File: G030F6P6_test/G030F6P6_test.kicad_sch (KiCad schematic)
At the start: 36 parts, among them J1 Conn_01x10_Female, J3 Conn_01x10_Female, J4 USB_C_Receptacle_USB2.0, J5 Conn_01x05_Female, SW1 SW_Push_SPDT, U1 CH343P, U2 STM32G030FxP, U3 XC6206P332MR

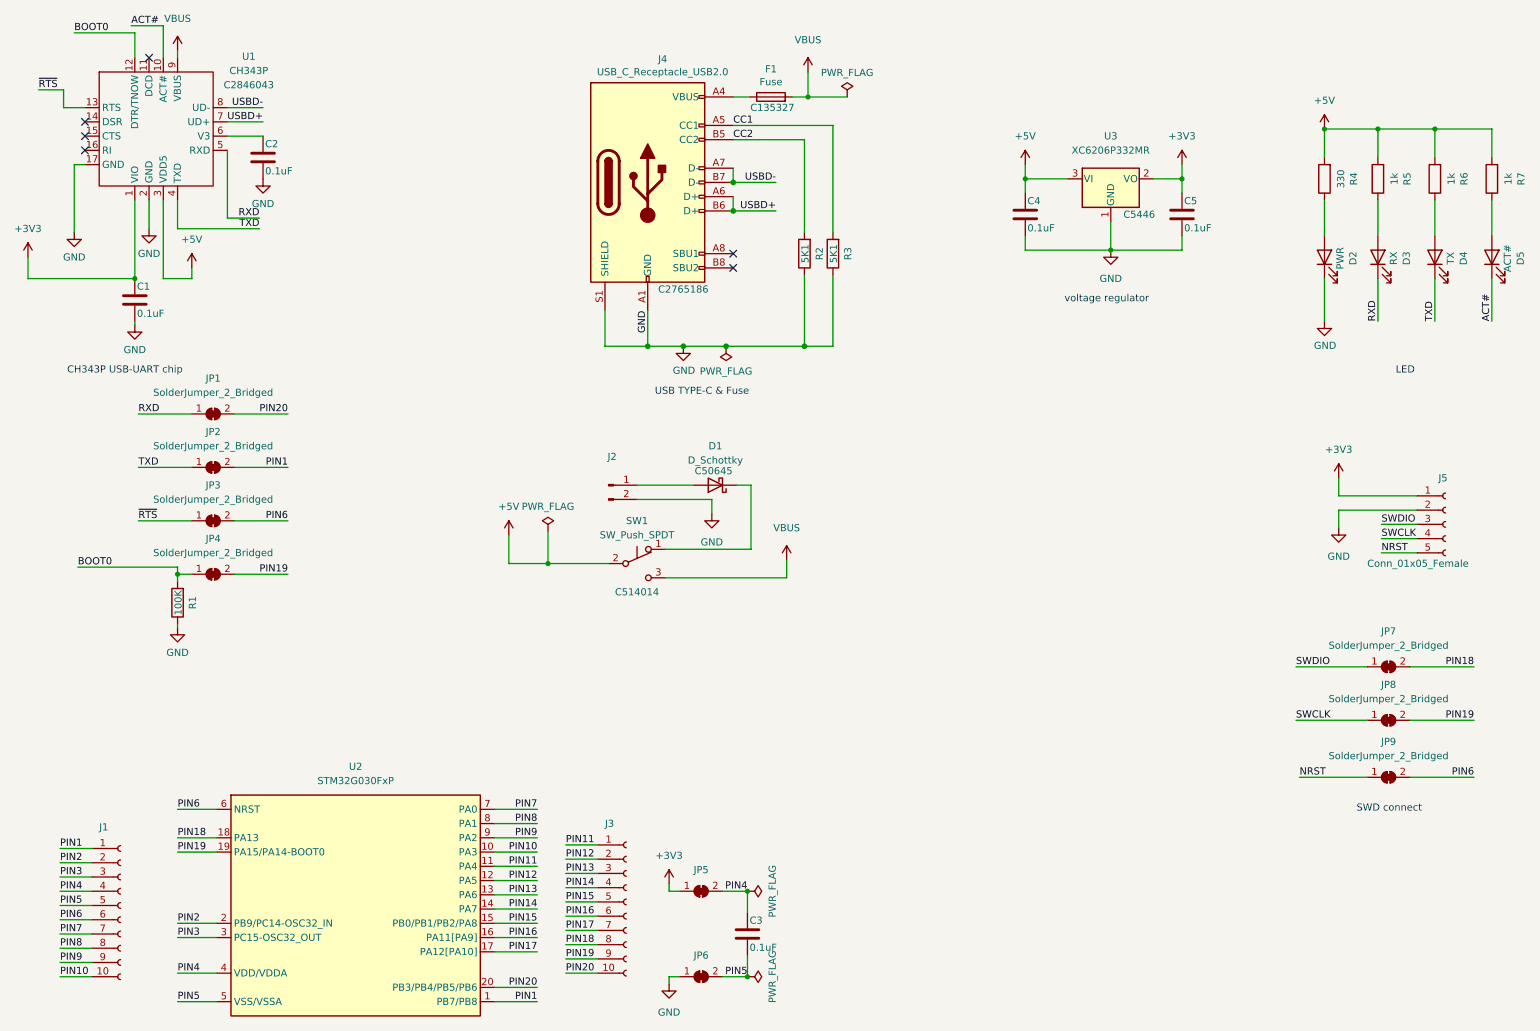
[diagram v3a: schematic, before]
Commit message: Update G030F6P6_test.kicad_sch
移除LED
更換 CH343P 封裝
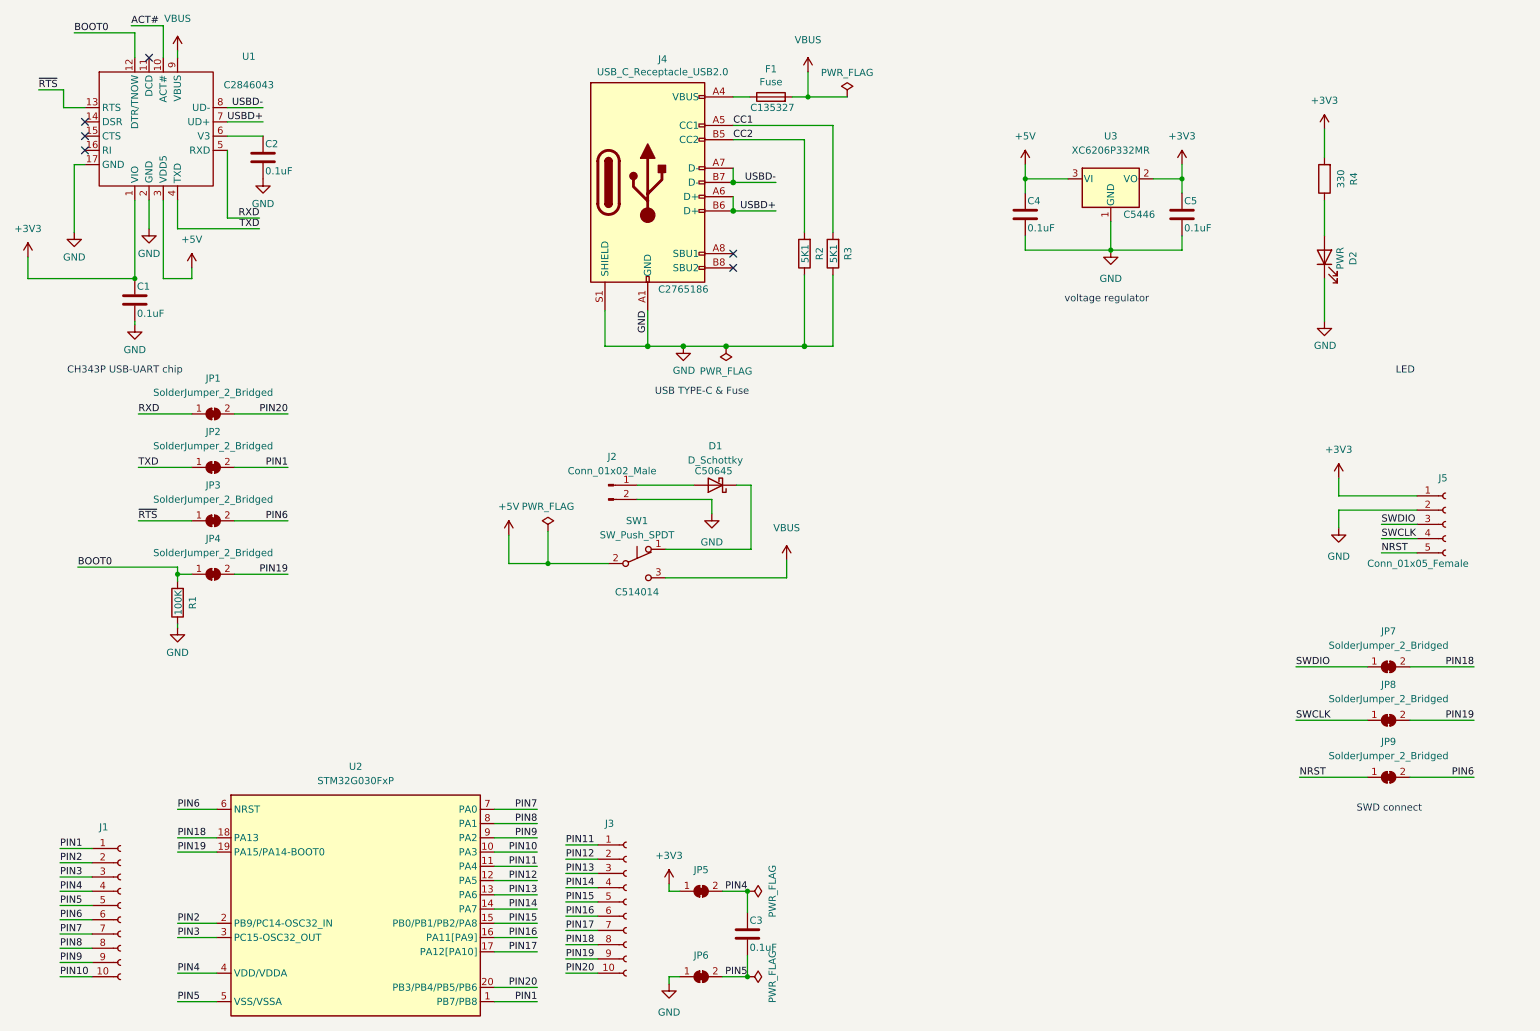
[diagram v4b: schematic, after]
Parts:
- removed D3: RX, LED_SMD:LED_0805_2012Metric, symbol Device:LED
- removed D4: TX, LED_SMD:LED_0805_2012Metric, symbol Device:LED
- removed D5: ACT#, LED_SMD:LED_0805_2012Metric, symbol Device:LED
- removed R5, R6, R7: 1k, Resistor_SMD:R_0805_2012Metric, symbol Device:R
- J2: value (none) -> Conn_01x02_Male; footprint (none) -> Connector_PinHeader_2.54mm:PinHeader_1x02_P2.54mm_Vertical
- U1: value CH343P -> (none); footprint Package_DFN_QFN:QFN-16-1EP_3x3mm_P0.5mm_EP1.45x1.45mm -> (none)
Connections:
- net +3V3: now also R4.2
- net +5V: no longer R4.2

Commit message: Update G030F6P6_test.kicad_sch
移除電壓選擇
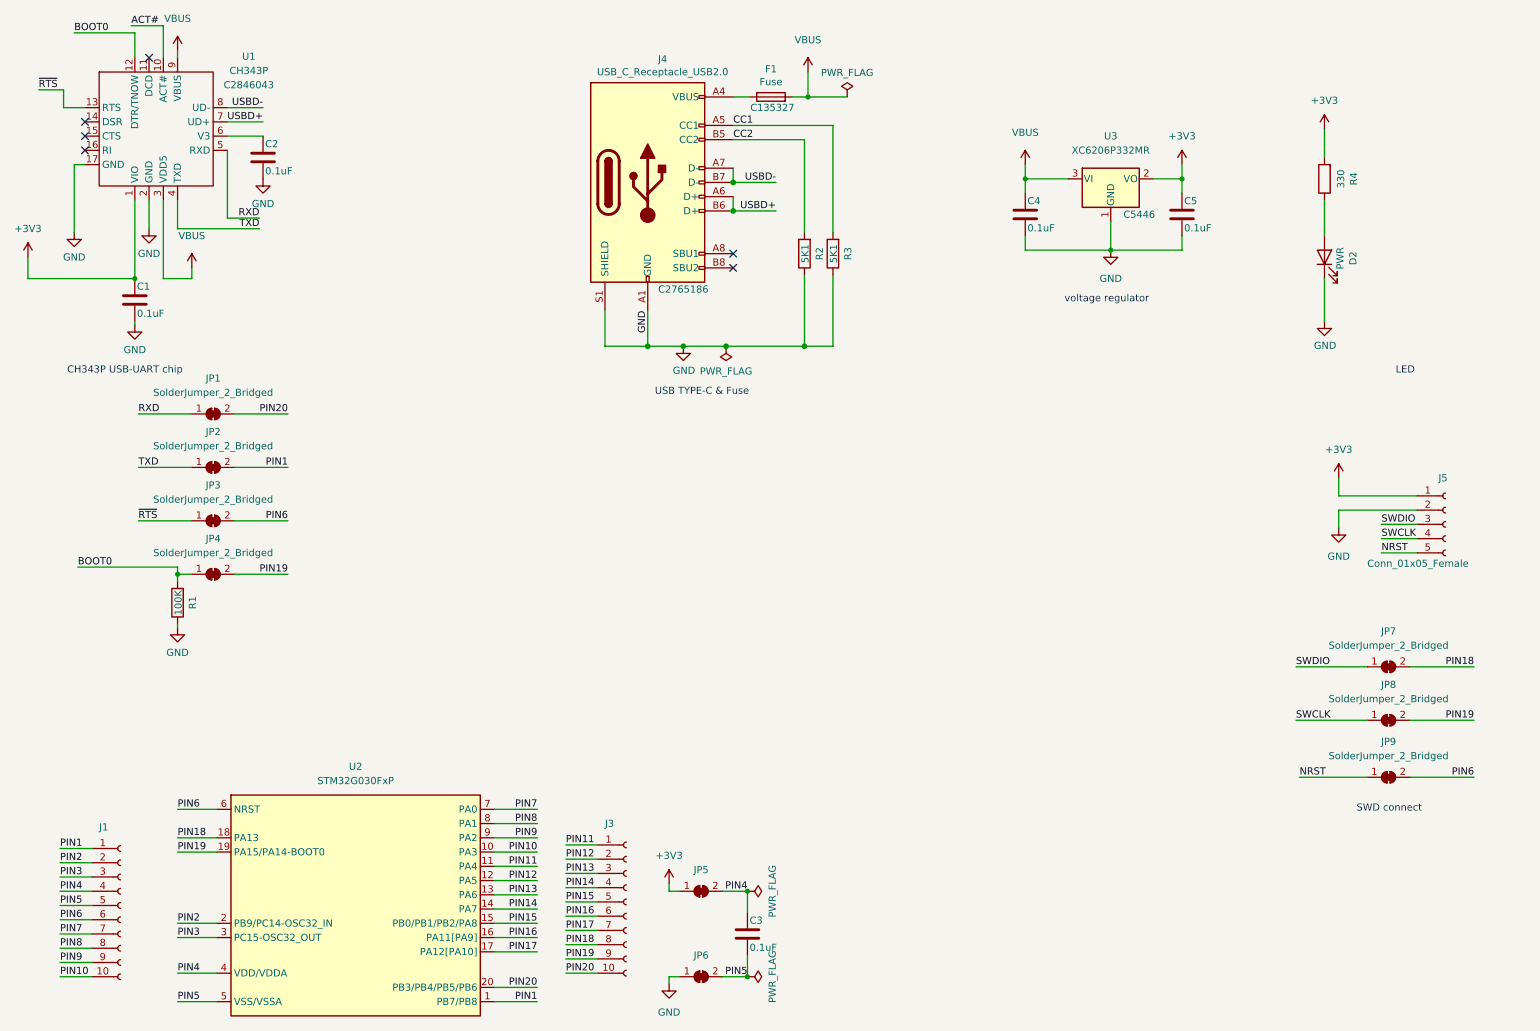
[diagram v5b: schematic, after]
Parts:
- removed D1: D_Schottky, Diode_SMD:D_SMA, symbol Device:D_Schottky
- removed J2: Conn_01x02_Male, Connector_PinHeader_2.54mm:PinHeader_1x02_P2.54mm_Vertical, symbol Connector:Conn_01x02_Male
- removed SW1: SW_Push_SPDT, Button_Switch_SMD:SW_SPDT_PCM12, symbol Switch:SW_Push_SPDT
- U1: value (none) -> CH343P; footprint (none) -> Package_DFN_QFN:QFN-16-1EP_3x3mm_P0.5mm_EP1.45x1.45mm_ThermalVias
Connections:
- net +5V is gone; now on net VBUS: C4.1, U1.3 (VDD5), U3.3 (VI)

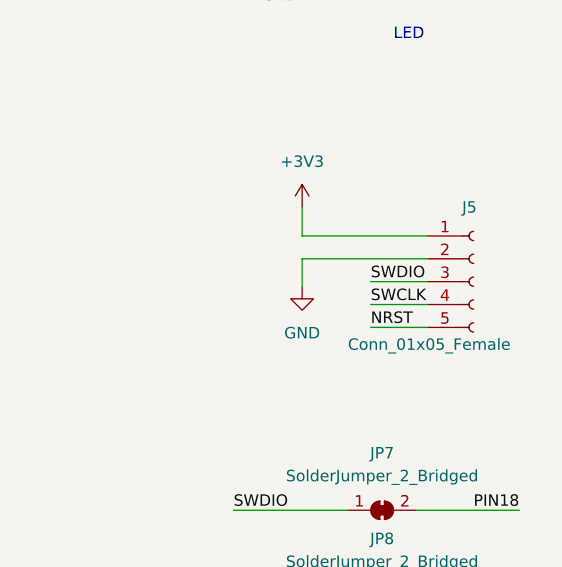
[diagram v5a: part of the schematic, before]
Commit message: Update G030F6P6_test.kicad_sch
交換 SWCLK 與 SWDIO
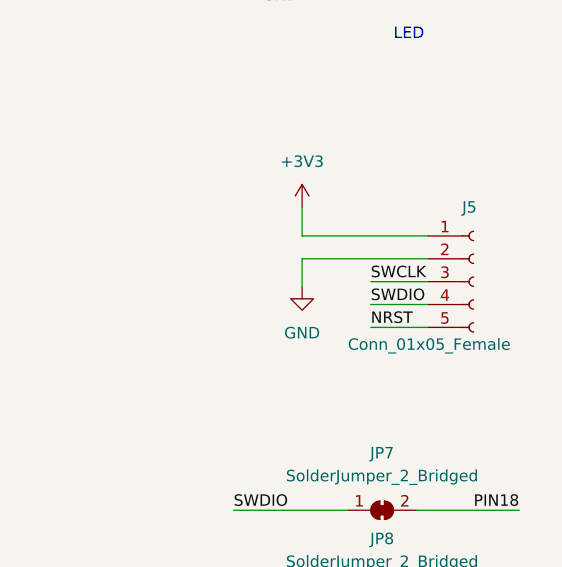
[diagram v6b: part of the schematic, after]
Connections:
- net SWCLK: now also J5.3 (Pin_3); no longer J5.4 (Pin_4)
- net SWDIO: now also J5.4 (Pin_4); no longer J5.3 (Pin_3)
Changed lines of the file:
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@@
     (effects (font (size 1.27 1.27)) (justify left bottom))
   )
-  (label "SWDIO" (at 259.08 106.045 0)
+  (label "SWCLK" (at 259.08 106.045 0)
     (effects (font (size 1.27 1.27)) (justify left bottom))
   )
@@
     (effects (font (size 1.27 1.27)) (justify right bottom))
   )
-  (label "SWCLK" (at 259.08 108.585 0)
+  (label "SWDIO" (at 259.08 108.585 0)
     (effects (font (size 1.27 1.27)) (justify left bottom))
   )

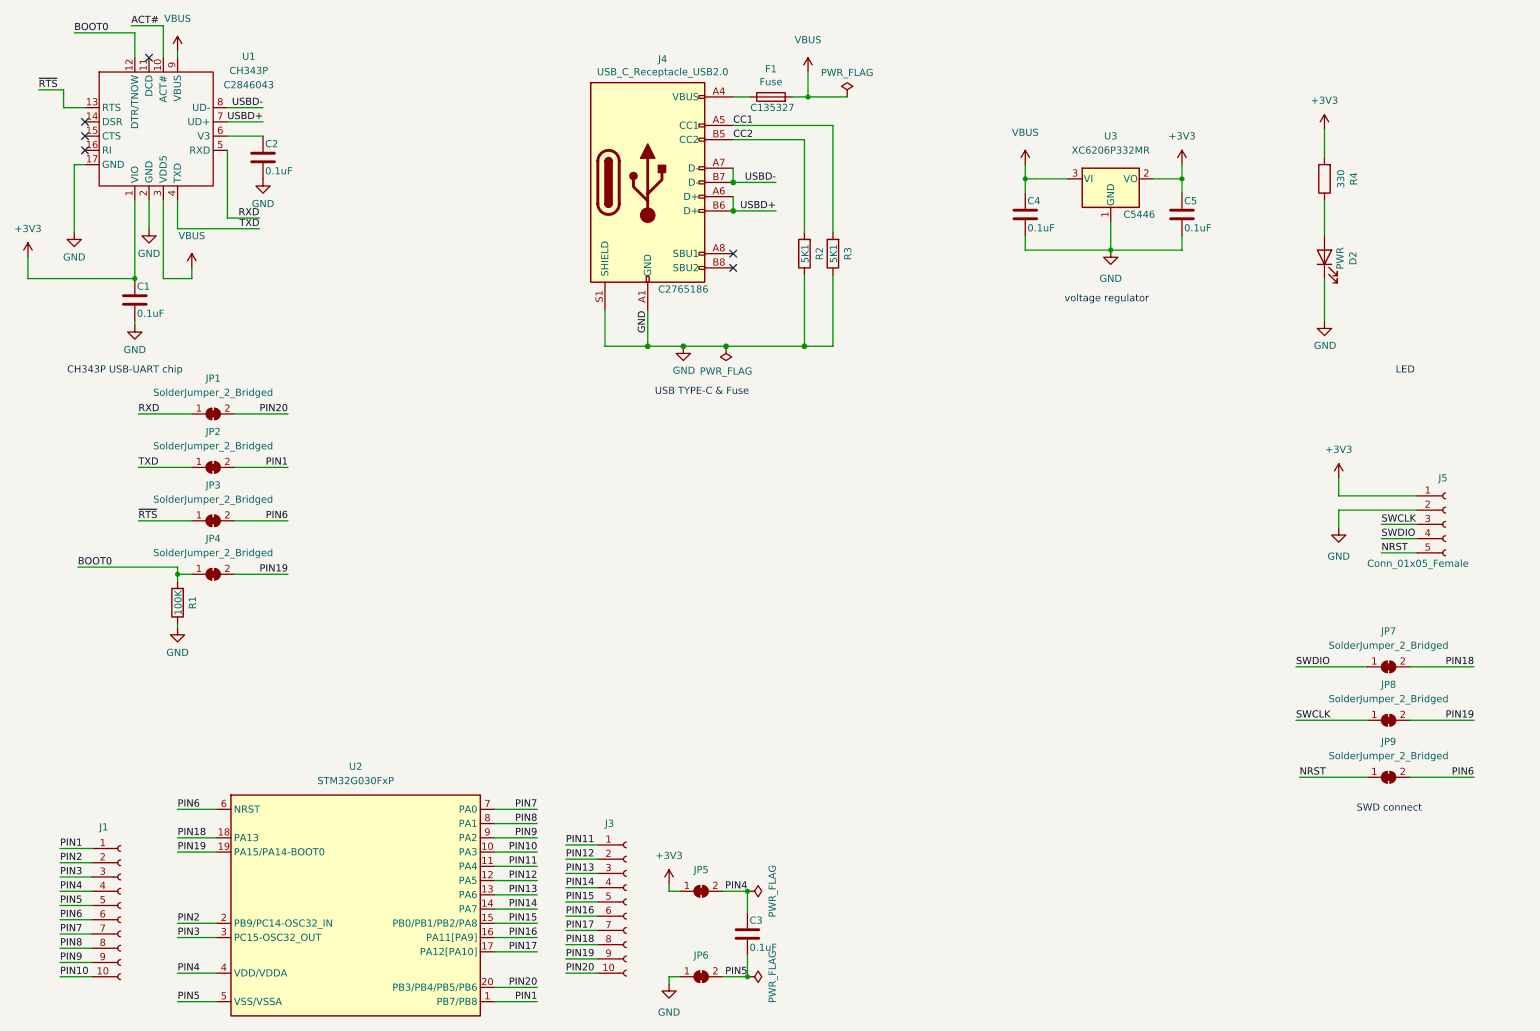
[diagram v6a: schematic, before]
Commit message: Update G030F6P6_test.kicad_sch
增加 5V 連接腳位
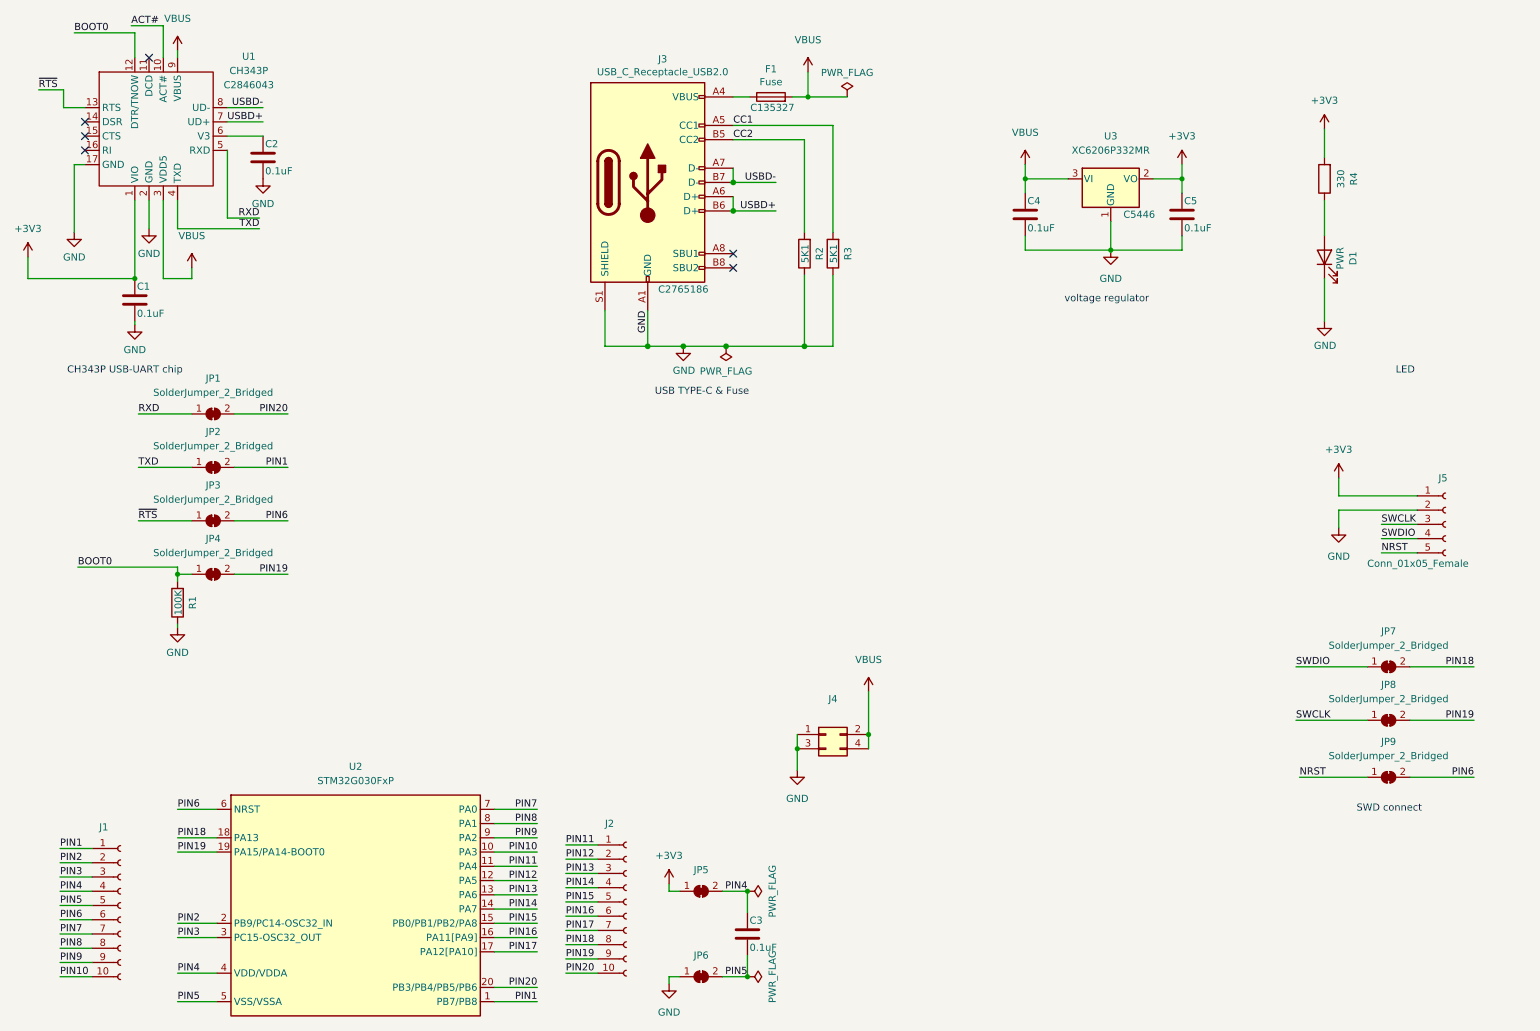
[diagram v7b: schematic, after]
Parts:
- added J4: (no value), symbol Connector_Generic:Conn_02x02_Odd_Even
- renumbered D2 to D1, J3 to J2, J4 to J3
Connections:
- net GND: now also J4.1 (Pin_1), J4.3 (Pin_3)
- net VBUS: now also J4.2 (Pin_2), J4.4 (Pin_4)
